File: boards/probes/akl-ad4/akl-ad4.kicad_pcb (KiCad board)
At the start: 4 copper layers, 17.8 x 10.8 mm, 33 parts, among them J1 U.FL, J2 TIPRES, J3 TIPRES, J4 SMPM, U1 ADP7142ACPZN-R7, U2 ADP7182_DFN8, U3 LMR70503, U4 ADL5569

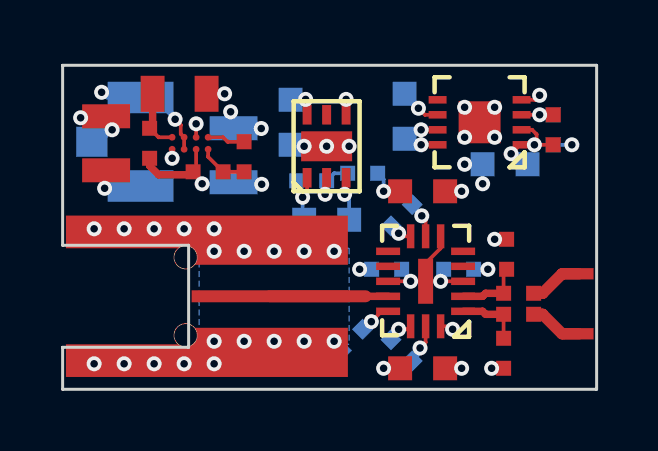
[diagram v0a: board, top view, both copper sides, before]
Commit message: Small tweaks to AKL-AD4 from design review. Ready for fab.
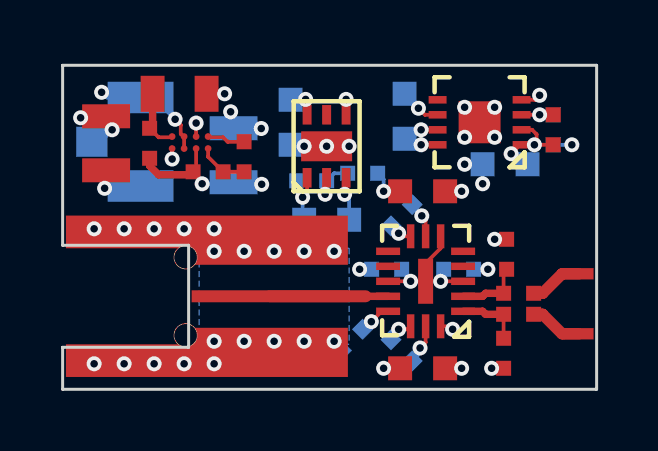
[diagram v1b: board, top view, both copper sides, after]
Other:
- board text added: "2022-06-11"
- board text added: "A. Zonenberg"
- board text added: "AKL-AD4 v0.1"
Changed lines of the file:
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@@
       (outputformat 1)
       (mirror false)
-      (drillshape 1)
+      (drillshape 0)
       (scaleselection 1)
-      (outputdirectory "")
+      (outputdirectory "output/")
     )
   )
@@
   )
   (footprint "azonenberg_pcb:BGA_8_1.65x0.865_0.4MM_TI_YFX" (layer "F.Cu")
-    (at 75.95 53.9 -90)
+    (at 75.95 53.875 -90)
     (property "Sheetfile" "akl-ad4.kicad_sch")
     (property "Sheetname" "")
@@
   (gr_line (start 71.7 60.7) (end 71.7 62.1) (layer "Edge.Cuts") (width 0.1))
   (gr_line (start 71.7 62.1) (end 89.5 62.1) (layer "Edge.Cuts") (width 0.1))
+  (gr_text "2022-06-11" (at 85.3 61.6) (layer "B.SilkS")
+    (effects (font (size 0.75 0.75) (thickness 0.1)) (justify mirror))
+  )
+  (gr_text "A. Zonenberg" (at 85.3 58.9) (layer "B.SilkS")
+    (effects (font (size 0.75 0.75) (thickness 0.1)) (justify mirror))
+  )
+  (gr_text "AKL-AD4 v0.1" (at 84.45 57.4) (layer "B.SilkS")
+    (effects (font (size 0.75 0.75) (thickness 0.1)) (justify mirror))
+  )
   (segment (start 76.35 55.15) (end 76.05 54.85) (width 0.125) (layer "F.Cu") (net 1))
   (segment (start 74.9 54.95) (end 75.9 54.95) (width 0.25) (layer "F.Cu") (net 1))
@@
   (segment (start 73.35 53.2) (end 73.15 53) (width 0.125) (layer "F.Cu") (net 3))
   (via (at 73.35 53.45) (size 0.5) (drill 0.25) (layers "F.Cu" "B.Cu") (net 3))
-  (via (at 75.35 54.4) (size 0.5) (drill 0.25) (layers "F.Cu" "B.Cu") (net 3))
-  (via (at 76.15 53.25) (size 0.5) (drill 0.25) (layers "F.Cu" "B.Cu") (net 3))
+  (via (at 75.35 54.425) (size 0.5) (drill 0.25) (layers "F.Cu" "B.Cu") (net 3))
+  (via (at 76.15 53.225) (size 0.5) (drill 0.25) (layers "F.Cu" "B.Cu") (net 3))
   (via (at 79.8 52.437) (size 0.5) (drill 0.25) (layers "F.Cu" "B.Cu") (net 3))
   (via (at 72.3 53.05) (size 0.5) (drill 0.25) (layers "F.Cu" "B.Cu") (net 3))

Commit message: Rev 0.2 of AKL-AD4
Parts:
- R7, R8: footprint azonenberg_pcb:EIA_0402_RES_NOSILK -> azonenberg_pcb:EIA_0201_RES_NOSILK
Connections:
- U4 pad 16: /2V5_P -> /GND
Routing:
- net /2V5_P: track 14.8 -> 12.6 mm, vias 5 -> 4
- net /GND: track 83.1 -> 84.9 mm, vias 42 -> 43
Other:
- board text added: "+"
- board text added: "2022-06-24"
- board text added: "AKL-AD4 v0.2"
- board text removed: "2022-06-11"
- board text removed: "AKL-AD4 v0.1"
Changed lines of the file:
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@@
       (net 2 "/GND") (pinfunction "VCOM") (pintype "input"))
     (pad "16" smd rect locked (at -0.5 -1.5 180) (size 0.25 0.8) (layers "F.Cu" "F.Paste" "F.Mask")
-      (net 5 "/2V5_P") (pinfunction "PBDB") (pintype "input"))
+      (net 2 "/GND") (pinfunction "PBDB") (pintype "input"))
     (pad "PAD" smd rect locked (at 0 0 180) (size 0.5 1.5) (layers "F.Cu" "F.Paste" "F.Mask")
       (net 4 "/2V5_N") (pinfunction "GND") (pintype "input"))
@@
     )
   )
-  (footprint "azonenberg_pcb:EIA_0402_RES_NOSILK" (layer "F.Cu")
+  (footprint "azonenberg_pcb:EIA_0201_RES_NOSILK" (layer "F.Cu")
     (at 86.9 58.9 180)
     (property "Sheetfile" "akl-ad4.kicad_sch")
     (property "Sheetname" "")
-    (attr smd)
-    (fp_text reference "R7" (at 0 1.5) (layer "F.SilkS") hide
-      (effects (font (size 1 1) (thickness 0.15)))
-    )
-    (fp_text value "348" (at 0 3.5) (layer "F.SilkS") hide
-      (effects (font (size 1 1) (thickness 0.15)))
-    )
-    (pad "1" smd rect (at -0.5 0 180) (size 0.5 0.5) (layers "F.Cu" "F.Paste" "F.Mask")
+    (attr through_hole)
+    (fp_text reference "R7" (at -0.05 0.75 180) (layer "F.SilkS") hide
+      (effects (font (size 0.508 0.457) (thickness 0.11)))
+    )
+    (fp_text value "348" (at 0.05 1.5 180) (layer "F.SilkS") hide
+      (effects (font (size 0.508 0.457) (thickness 0.11)))
+    )
+    (pad "1" smd rect locked (at -0.22 0 180) (size 0.21 0.3) (layers "F.Cu" "F.Paste" "F.Mask")
       (net 8 "Net-(J3-Pad1)") (pintype "passive"))
-    (pad "2" smd rect (at 0.5 0 180) (size 0.5 0.5) (layers "F.Cu" "F.Paste" "F.Mask")
+    (pad "2" smd rect locked (at 0.22 0 180) (size 0.21 0.3) (layers "F.Cu" "F.Paste" "F.Mask")
       (net 14 "/VIN_P") (pintype "passive"))
-    (model ":walter:smd_resistors/r_0402.wrl"
-      (offset (xyz 0 0 0))
-      (scale (xyz 1 1 1))
-      (rotate (xyz 0 0 0))
-    )
-  )
-  (footprint "azonenberg_pcb:EIA_0402_RES_NOSILK" (layer "F.Cu")
+    (model "/nfs4/home/azonenberg/kicad-libs/3rdparty/walter/smd_resistors/r_0402.wrl"
+      (offset (xyz 0 0 0))
+      (scale (xyz 0.5 0.5 0.5))
+      (rotate (xyz 0 0 0))
+    )
+  )
+  (footprint "azonenberg_pcb:EIA_0201_RES_NOSILK" (layer "F.Cu")
     (at 86.9 59.6 180)
     (property "Sheetfile" "akl-ad4.kicad_sch")
     (property "Sheetname" "")
-    (attr smd)
-    (fp_text reference "R8" (at 0 1.5) (layer "F.SilkS") hide
-      (effects (font (size 1 1) (thickness 0.15)))
-    )
-    (fp_text value "348" (at 0 3.5) (layer "F.SilkS") hide
-      (effects (font (size 1 1) (thickness 0.15)))
-    )
-    (pad "1" smd rect (at -0.5 0 180) (size 0.5 0.5) (layers "F.Cu" "F.Paste" "F.Mask")
+    (attr through_hole)
+    (fp_text reference "R8" (at -0.05 0.75 180) (layer "F.SilkS") hide
+      (effects (font (size 0.508 0.457) (thickness 0.11)))
+    )
+    (fp_text value "348" (at 0.05 1.5 180) (layer "F.SilkS") hide
+      (effects (font (size 0.508 0.457) (thickness 0.11)))
+    )
+    (pad "1" smd rect locked (at -0.22 0 180) (size 0.21 0.3) (layers "F.Cu" "F.Paste" "F.Mask")
       (net 7 "Net-(J2-Pad1)") (pintype "passive"))
-    (pad "2" smd rect (at 0.5 0 180) (size 0.5 0.5) (layers "F.Cu" "F.Paste" "F.Mask")
+    (pad "2" smd rect locked (at 0.22 0 180) (size 0.21 0.3) (layers "F.Cu" "F.Paste" "F.Mask")
       (net 15 "/VIN_N") (pintype "passive"))
-    (model ":walter:smd_resistors/r_0402.wrl"
-      (offset (xyz 0 0 0))
-      (scale (xyz 1 1 1))
+    (model "/nfs4/home/azonenberg/kicad-libs/3rdparty/walter/smd_resistors/r_0402.wrl"
+      (offset (xyz 0 0 0))
+      (scale (xyz 0.5 0.5 0.5))
       (rotate (xyz 0 0 0))
     )
@@
   (gr_line (start 71.7 60.7) (end 71.7 62.1) (layer "Edge.Cuts") (width 0.1))
   (gr_line (start 71.7 62.1) (end 89.5 62.1) (layer "Edge.Cuts") (width 0.1))
-  (gr_text "2022-06-11" (at 85.3 61.6) (layer "B.SilkS")
+  (gr_text "2022-06-24" (at 85.3 61.6) (layer "B.SilkS")
     (effects (font (size 0.75 0.75) (thickness 0.1)) (justify mirror))
   )
@@
     (effects (font (size 0.75 0.75) (thickness 0.1)) (justify mirror))
   )
-  (gr_text "AKL-AD4 v0.1" (at 84.45 57.4) (layer "B.SilkS")
+  (gr_text "AKL-AD4 v0.2" (at 84.45 57.4) (layer "B.SilkS")
     (effects (font (size 0.75 0.75) (thickness 0.1)) (justify mirror))
+  )
+  (gr_text "+" (at 88.9 57.404) (layer "F.SilkS")
+    (effects (font (size 0.75 0.75) (thickness 0.1)))
   )
   (segment (start 76.35 55.15) (end 76.05 54.85) (width 0.125) (layer "F.Cu") (net 1))
@@
   (segment (start 84.2 52.95) (end 83.777921 52.95) (width 0.125) (layer "F.Cu") (net 2))
   (segment (start 76.5 52.25) (end 77.1 52.25) (width 0.125) (layer "F.Cu") (net 2))
+  (segment (start 84.6 60) (end 84.7 60.1) (width 0.125) (layer "F.Cu") (net 2))
+  (segment (start 84.3 60) (end 84.6 60) (width 0.125) (layer "F.Cu") (net 2))
   (segment (start 83.8 57) (end 83.8 56.446548) (width 0.125) (layer "F.Cu") (net 2))
   (segment (start 84.45 61.4) (end 85 61.4) (width 0.125) (layer "F.Cu") (net 2))
@@
   (via (at 83.6137 60.723486) (size 0.5) (drill 0.25) (layers "F.Cu" "B.Cu") (net 2))
   (via (at 83.671611 56.318159) (size 0.5) (drill 0.25) (layers "F.Cu" "B.Cu") (net 2))
+  (via (at 84.7 60.1) (size 0.5) (drill 0.25) (layers "F.Cu" "B.Cu") (net 2))
   (via (at 86.1 57.1) (size 0.5) (drill 0.25) (layers "F.Cu" "B.Cu") (net 2))
   (via (at 76.75 60.5) (size 0.5) (drill 0.25) (layers "F.Cu" "B.Cu") (net 2))
@@
   (segment (start 83.560061 52.73214) (end 83.88214 52.73214) (width 0.125) (layer "In1.Cu") (net 2))
   (segment (start 73.9 53.1) (end 73.85 53.05) (width 0.125) (layer "In1.Cu") (net 2))
+  (segment (start 83.6137 60.723486) (end 84.237186 60.1) (width 0.125) (layer "In1.Cu") (net 2))
   (segment (start 85 61.4) (end 84.290214 61.4) (width 0.125) (layer "In1.Cu") (net 2))
   (segment (start 78.321132 53.407321) (end 77.763811 52.85) (width 0.125) (layer "In1.Cu") (net 2))
@@
   (segment (start 73.85 55.4) (end 73.1 55.4) (width 0.125) (layer "In1.Cu") (net 2))
   (segment (start 83.8 57.9) (end 83.8 56.446548) (width 0.125) (layer "In1.Cu") (net 2))
+  (segment (start 84.237186 60.1) (end 84.7 60.1) (width 0.125) (layer "In1.Cu") (net 2))
   (segment (start 81.35 58.1) (end 80.75 57.5) (width 0.125) (layer "In1.Cu") (net 2))
   (segment (start 82.853452 55.5) (end 83.671611 56.318159) (width 0.125) (layer "In1.Cu") (net 2))
@@
   (segment (start 83 57) (end 82.9 56.9) (width 0.125) (layer "F.Cu") (net 5))
   (segment (start 79.85 55.55) (end 79.7 55.7) (width 0.125) (layer "F.Cu") (net 5))
-  (segment (start 84.6 60) (end 84.7 60.1) (width 0.125) (layer "F.Cu") (net 5))
-  (segment (start 84.3 60) (end 84.6 60) (width 0.125) (layer "F.Cu") (net 5))
-  (via (at 84.7 60.1) (size 0.5) (drill 0.25) (layers "F.Cu" "B.Cu") (net 5))
   (via (at 79.7 55.7) (size 0.5) (drill 0.25) (layers "F.Cu" "B.Cu") (net 5))
   (via (at 82.4 61.4) (size 0.5) (drill 0.25) (layers "F.Cu" "B.Cu") (net 5))
@@
   (segment (start 79.7 55.7) (end 79.7 56.45) (width 0.125) (layer "In2.Cu") (net 5))
   (segment (start 82.9 56.9) (end 82.7 57.1) (width 0.125) (layer "In2.Cu") (net 5))
-  (segment (start 84.7 60.1) (end 82.9 60.1) (width 0.125) (layer "In2.Cu") (net 5))
   (segment (start 82.4 61.4) (end 82.4 60.6) (width 0.125) (layer "In2.Cu") (net 5))
   (segment (start 82.7 59.9) (end 82.9 60.1) (width 0.125) (layer "In2.Cu") (net 5))
@@
   (segment (start 87.7 59.6) (end 87.4 59.6) (width 0.38) (layer "F.Cu") (net 7))
   (segment (start 88.9 60.25) (end 88.35 60.25) (width 0.38) (layer "F.Cu") (net 7))
+  (segment (start 87.4 59.6) (end 87.12 59.6) (width 0.25) (layer "F.Cu") (net 7))
+  (segment (start 87.4 58.9) (end 87.12 58.9) (width 0.25) (layer "F.Cu") (net 8))
   (segment (start 88.35 58.25) (end 87.7 58.9) (width 0.38) (layer "F.Cu") (net 8))
   (segment (start 88.9 58.25) (end 88.35 58.25) (width 0.38) (layer "F.Cu") (net 8))
@@
   (segment (start 85.05 59) (end 85.7 59) (width 0.25) (layer "F.Cu") (net 14))
   (segment (start 86.4 58.2) (end 86.5 58.1) (width 0.125) (layer "F.Cu") (net 14))
+  (segment (start 86.4 58.9) (end 86.68 58.9) (width 0.25) (layer "F.Cu") (net 14))
   (segment (start 86.4 58.9) (end 86.4 58.2) (width 0.125) (layer "F.Cu") (net 14))
   (segment (start 85.7 59.5) (end 85.8 59.6) (width 0.25) (layer "F.Cu") (net 15))
   (segment (start 86.4 59.6) (end 86.4 60.4) (width 0.125) (layer "F.Cu") (net 15))
+  (segment (start 86.4 59.6) (end 86.68 59.6) (width 0.25) (layer "F.Cu") (net 15))
   (segment (start 85.8 59.6) (end 86.4 59.6) (width 0.25) (layer "F.Cu") (net 15))
   (segment (start 85.05 59.5) (end 85.7 59.5) (width 0.25) (layer "F.Cu") (net 15))

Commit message: Updated AKL-AD4 v0.3
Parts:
- added C13: 0.47 uF, azonenberg_pcb:EIA_0402_CAP_NOSILK, B.Cu at (85.8, 61.0)
- added R12: 470, azonenberg_pcb:EIA_0402_RES_NOSILK, B.Cu at (88.4, 52.8)
- added R13: 3312J-1-200E, azonenberg_pcb:RES_TRIM_BOURNS_3312, F.Cu at (87.8, 53.6)
- added R14: 470, azonenberg_pcb:EIA_0402_RES_NOSILK, B.Cu at (86.2, 51.8)
- added U5: EQY-1-63+, azonenberg_pcb:DFN_8_0.5MM_2x2MM, F.Cu at (81.5, 58.8)
- J4: footprint azonenberg_pcb:CONN_SMPM_AMPHENOL_925-169J-51PT -> azonenberg_pcb:CONN_SMPM_AMPHENOL_925-169J-51PT_SHORT
- R1: moved to B.Cu
- moved C4 1.41 mm to (85.0, 54.8)
- moved C1 1.30 mm to (81.8, 53.1)
- moved R2 1.30 mm to (86.8, 53.5)
- moved U2 1.30 mm to (84.3, 53.3)
- moved R7 1.26 mm to (88.0, 58.2)
- moved R8 1.26 mm to (88.0, 60.2)
- moved C11 1.20 mm to (84.2, 56.4)
- moved C12 1.20 mm to (83.7, 58.1)
- moved C7 1.20 mm to (84.9, 61.4)
- moved R11 1.20 mm to (82.5, 60.5)
- moved U4 1.20 mm to (85.0, 58.5)
- moved C10 1.20 mm to (86.1, 58.1)
- moved R10 0.93 mm to (87.3, 60.9)
- moved R9 0.80 mm to (87.3, 57.7)
- moved R1 0.56 mm to (87.5, 53.5)
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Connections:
- J4 pad 1: /VOUT -> /VOUT_EQ
- U4 pad 15: /GND -> /VCOM
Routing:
- net /GND: track 84.9 -> 70.4 mm
- net /2V5_P: track 12.6 -> 21.3 mm
- net /VCOM: track 0.00 -> 8.58 mm, vias 0 -> 2
- net /2V5_N: track 15.5 -> 20.2 mm, vias 5 -> 7
- net /VOUT_EQ: track 0.00 -> 2.84 mm
- net /VOUT: track 3.94 -> 1.30 mm
- net Net-(J3-Pad1): track 2.05 -> 0.55 mm
- net Net-(J2-Pad1): track 2.05 -> 0.55 mm
- net /3V5: track 19.6 -> 18.2 mm
- net /3V5_N: track 27.8 -> 26.5 mm
- net Net-(R13-Pad3): track 0.00 -> 1.11 mm, vias 0 -> 1
- net Net-(R12-Pad1): track 0.00 -> 0.61 mm, vias 0 -> 1
- net Net-(R11-Pad1): track 1.10 -> 0.49 mm
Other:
- board text added: "2022-07-10"
- board text added: "3.5V"
- board text added: "AKL-AD4"
- board text added: "v0.3"
- board text removed: "2022-06-24"
- board text removed: "AKL-AD4 v0.2"

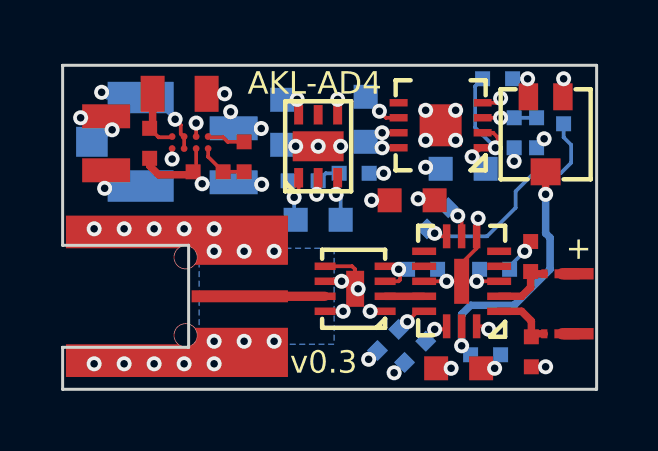
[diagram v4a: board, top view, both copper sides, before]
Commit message: AKL-AD4: rev 0.4 with LM27761 based power stage, 2.5mm shorter, improved heatsinking, removed equalizer
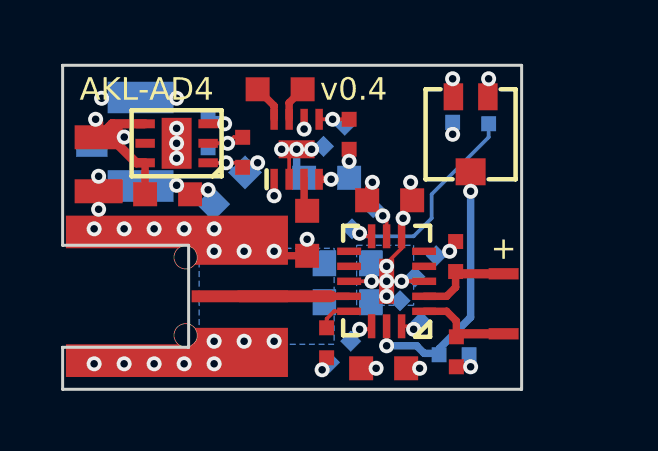
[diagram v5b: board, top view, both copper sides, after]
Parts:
- removed D1: VSKY05201006-G4-08, azonenberg_pcb:EIA_0402_CAP_NOSILK
- removed L1: LQM21PN4R7MGHL, azonenberg_pcb:EIA_0805_INDUCTOR_NOSILK
- removed R3: 100K, azonenberg_pcb:EIA_0402_RES_NOSILK
- removed R6: 294K, azonenberg_pcb:EIA_0402_RES_NOSILK
- removed R7, R8: 348, azonenberg_pcb:EIA_0201_RES_NOSILK
- removed U3: LMR70503, azonenberg_pcb:BGA_8_1.65x0.865_0.4MM_TI_YFX
- removed U5: EQY-1-63+, azonenberg_pcb:DFN_8_0.5MM_2x2MM
- added TJ1: THERMAL_JUMPER, azonenberg_pcb:EIA_0603_RES_NOSILK, B.Cu at (81.2, 57.9)
- added TJ2: THERMAL_JUMPER, azonenberg_pcb:EIA_0603_RES_NOSILK, B.Cu at (81.2, 59.2)
- C1, C3, R11, R4: moved to F.Cu
- C4: value 4.7 uF -> 1 uF; moved to F.Cu
- C6: value 22 uF -> 4.7 uF; footprint azonenberg_pcb:EIA_0805_CAP_NOSILK -> azonenberg_pcb:EIA_0603_CAP_NOSILK
- R1: value 100K -> 93.1K; moved to F.Cu
- R2: value 95.3K -> 88.7K
- U2: value ADP7182_DFN8 -> LM27761; footprint azonenberg_pcb:DFN_8_0.5MM_3x3MM -> azonenberg_pcb:DFN_8_0.5MM_2x2MM
- moved C4 6.65 mm to (79.0, 52.1), turned to 180 degrees
- moved R1 6.25 mm to (81.2, 53.6)
- moved R2 6.00 mm to (80.8, 53.6), turned to -135 degrees
- moved R5 5.05 mm to (76.5, 53.5), turned to 90 degrees
- moved U2 4.87 mm to (79.5, 54.1)
- moved U1 4.72 mm to (75.5, 53.9), turned to 90 degrees
- moved C3 4.51 mm to (75.2, 55.6), turned to 180 degrees
- moved C1 4.27 mm to (79.8, 56.9)
- moved C6 3.19 mm to (80.5, 55.0), turned to 180 degrees
- moved C5 3.15 mm to (77.2, 55.4), turned to 45 degrees
- moved C11 2.50 mm to (81.7, 56.4)
- moved C7 2.50 mm to (82.4, 61.4)
- moved C9 2.50 mm to (81.0, 60.9)
- moved J2 2.50 mm to (86.4, 60.2)
- moved J3 2.50 mm to (86.4, 58.2)
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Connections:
- C1 pad 1: /3V5_N -> /GND
- C1 pad 2: /GND -> Net-(C1-Pad2)
- C4 pad 1: /GND -> Net-(C4-Pad1)
- C4 pad 2: /2V5_N -> Net-(C4-Pad2)
- C6 pad 1: /3V5_N -> /2V5_N
- J2 pad 1: Net-(J2-Pad1) -> /VIN_N
- J3 pad 1: Net-(J3-Pad1) -> /VIN_P
- J4 pad 1: /VOUT_EQ -> /VOUT
- U2 pad 1: /2V5_N -> /3V5
- U2 pad 2: /2V5_N -> /GND
- U2 pad 3: /2V5_N_FB -> Net-(C1-Pad2)
- U2 pad 4: /3V5_N -> /2V5_N
- U2 pad 5: (no net) -> /2V5_N_FB
- U2 pad 6: /GND -> /3V5
- U2 pad 7: /3V5_N -> Net-(C4-Pad1)
- U2 pad 8: /3V5_N -> Net-(C4-Pad2)
- U2 pad PAD: /3V5_N -> /GND
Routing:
- net /3V5_N: track 26.5 -> 0.00 mm, vias 9 -> 0
- net /GND: track 70.4 -> 61.2 mm, vias 43 -> 37
- net /3V5: track 18.2 -> 23.8 mm, vias 6 -> 4
- net /2V5_N: track 20.2 -> 16.2 mm, vias 7 -> 10
- net /2V5_P: track 21.3 -> 24.1 mm, vias 4 -> 5
- net /VOUT_EQ: track 2.84 -> 0.00 mm
- net /VOUT: track 1.30 -> 3.64 mm
- net Net-(D1-Pad1): track 1.92 -> 0.00 mm
- net Net-(R3-Pad2): track 1.66 -> 0.00 mm
- net /VIN_N: track 2.06 -> 3.35 mm
- net Net-(R3-Pad1): track 1.26 -> 0.00 mm
- net /VIN_P: track 2.08 -> 3.33 mm
- net Net-(C4-Pad2): track 0.00 -> 1.23 mm
- net Net-(C4-Pad1): track 0.00 -> 1.19 mm
- net Net-(C1-Pad2): track 0.00 -> 1.09 mm
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- added copper zone on B.Cu, net /2V5_N
- added copper zone on B.Cu, net /MOUNT_FOOT
- removed copper zone on B.Cu, net (none)
- removed copper zone on In2.Cu, net /3V5_N
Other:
- board size 17.8 x 10.8 mm -> 15.3 x 10.8 mm
- board text added: "2022-08-01"
- board text added: "v0.4"
- board text removed: "2022-07-10"
- board text removed: "v0.3"
